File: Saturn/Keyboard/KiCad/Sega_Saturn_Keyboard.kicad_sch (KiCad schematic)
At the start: 88 parts, among them SW1 RH CTRL, SW10 PRINT SCREEN, SW11 SCROLL LOCK, SW12 PAUSE, SW13 ? /, SW14 _ \, SW15 UP, SW16 LEFT, SW17 DOWN, SW18 RIGHT, SW19 PAGE DOWN, SW2 LH CTRL, SW20 PAGE UP, SW21 > ., SW22 無変換, SW23 カタカナ, SW24 前候補, SW25 SPACE, SW26 Z, SW27 END, SW28 K, SW29 L, SW3 RH SHIFT, SW30 + ;, SW31 * :, SW32 } ], SW33 ENTER, SW34 X, SW35 HOME, SW36 I, SW37 O, SW38 P, SW39 ' @, SW4 LH SHIFT, SW40 { [, SW41 DELETE, SW42 A, SW43 INSERT, SW44 ( 8, SW45 ) 9, SW46 ~ 0, SW47 = -, SW48 _ ^, SW49 | ¥, SW5 F8, SW50 S, SW51 BACKSPACE, SW52 < ,, SW53 M, SW54 N, SW55 B, SW56 V, SW57 C, SW58 J, SW59 H, SW6 F9, SW60 G, SW61 F, SW62 D, SW63 CAPS LOCK, SW64 U, SW65 Y, SW66 T, SW67 R, SW68 W, SW69 TAB, SW7 F10, SW70 E, SW71 半角/全角, SW72 ' 7, SW73 & 6, SW74 % 5, SW75 $ 4, SW76 # 3, SW77 " 2, SW78 Q, SW79 ! 1, SW8 F11, SW80 F7, SW81 F6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

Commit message: Initial PCB routing completed
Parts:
- added C1: 10µF, Capacitor_THT:CP_Radial_D8.0mm_P2.50mm, symbol Device:C_Polarized
- added CN1: Saturn, Connector_Dsub:DSUB-9_Pins_Horizontal_P2.77x2.84mm_EdgePinOffset7.70mm_Housed_MountingHolesOffset9.12mm, symbol Connector:DE9_Pins_MountingHoles
- added H1, H2, H3, H4, H5, H6: MountingHole, MountingHole:MountingHole_3.2mm_M3, symbol Mechanical:MountingHole
- added RN1: 10KΩ, Resistor_THT:R_Array_SIP9, symbol Device:R_Network08
- added RN2: R_Network07, Resistor_THT:R_Array_SIP8, symbol Device:R_Network07
- added SW84: F3, PCM_Switch_Keyboard_Cherry_MX:SW_Cherry_MX_PCB_1.00u, symbol Switch:SW_Push_45deg
- added U1: Teensy4.1, Clueless_Engineer:Teensy41, symbol teensy:Teensy4.1
- renumbered SW84 to SW85, SW85 to SW86, SW86 to SW87, SW87 to SW88, SW88 to SW89
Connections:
- net COL 16: now also RN1.2 (R1), U1.24 (32_OUT1B)
- net COL 17: now also RN1.3 (R2), U1.23 (31_CTX3)
- net COL 18: now also RN1.4 (R3), U1.22 (30_CRX3)
- net COL 19: now also RN1.5 (R4), SW84.1, U1.21 (29_TX7)
- net COL 20: now also RN1.6 (R5), U1.20 (28_RX7)
- net COL 21: now also RN1.7 (R6), U1.19 (27_A13_SCK1)
- net COL 22: now also RN1.8 (R7), U1.18 (26_A12_MOSI1)
- net COL 23: now also RN1.9 (R8), U1.17 (25_A11_RX6_SDA2)
- net ROW 1: now also U1.45 (23_A9_CRX1_MCLK1)
- net ROW 10: now also U1.8 (6_OUT1D)
- net ROW 11: now also U1.7 (5_IN2)
- net ROW 12: now also U1.6 (4_BCLK2)
- net ROW 13: now also SW84.2, U1.5 (3_LRCLK2)
- net ROW 14: now also U1.44 (22_A8_CTX1)
- net ROW 2: now also U1.43 (21_A7_RX5_BCLK1)
- net ROW 3: now also U1.11 (9_OUT1C)
- net ROW 4: now also U1.14 (12_MISO_MQSL)
- net ROW 5: now also U1.4 (2_OUT2)
- net ROW 6: now also U1.13 (11_MOSI_CTX1)
- net ROW 7: now also U1.12 (10_CS_MQSR)
- net ROW 8: now also U1.10 (8_TX2_IN1)
- net ROW 9: now also U1.9 (7_RX2_OUT1A)
- new net +5V_{OUT}: C1.1, CN1.1, RN1.1 (common), RN2.1 (common), U1.48 (VIN)
- new net D_{D1}: CN1.2, RN2.3 (R2), U1.30 (38_CS1_IN1)
- new net GND: C1.2, CN1.0 (PAD), CN1.9, U1.1 (GND), U1.34 (GND), U1.47 (GND), U1.52 (GND)
- new net L_{D2}: CN1.8, RN2.6 (R5), U1.27 (35_TX8)
- new net R_{D3}: CN1.7, RN2.4 (R3), U1.29 (37_CS)
- new net TH_{S0}: CN1.4, RN2.7 (R6), U1.26 (34_RX8)
- new net TL: CN1.6, RN2.2 (R1), U1.31 (39_MISO1_OUT1A)
- new net TR_{S1}: CN1.5, RN2.8 (R7), U1.25 (33_MCLK2)
- new net U_{D0}: CN1.3, RN2.5 (R4), U1.28 (36_CS)
- no-connect marks 0 -> 13

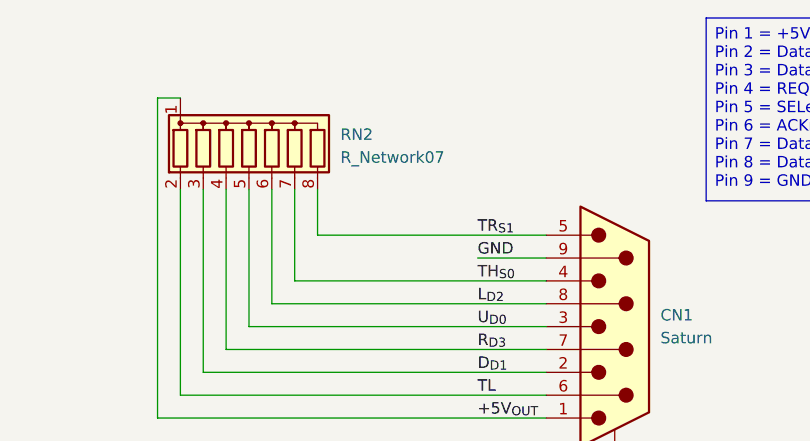
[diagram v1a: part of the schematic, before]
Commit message: Added 100KΩ value for pull-up
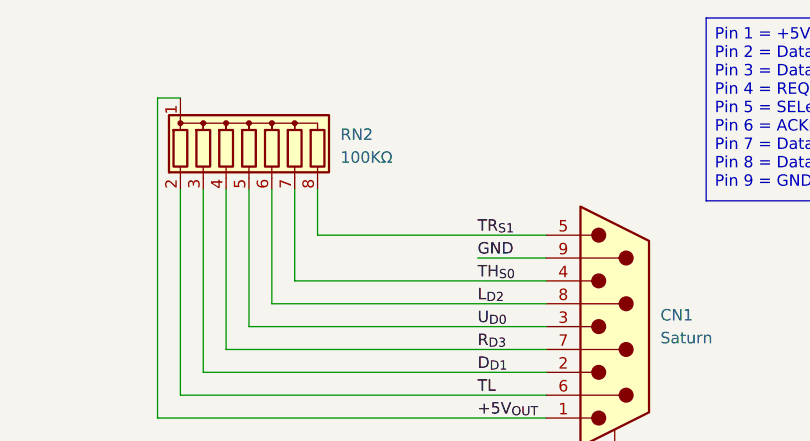
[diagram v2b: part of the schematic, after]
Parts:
- RN2: value R_Network07 -> 100KΩ
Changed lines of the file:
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@@
 			)
 		)
-		(property "Value" "R_Network07"
+		(property "Value" "100KΩ"
 			(at 334.01 32.0039 0)
 			(effects

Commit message: Additional text on PCB
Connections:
- no-connect marks 13 -> 28
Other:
- moved on the sheet: CN1, H1, H2, H3, H4, H5, H6, RN2

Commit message: Update Sega_Saturn_Keyboard.kicad_sch
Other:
- note added: "-->"
- note added: "<--"
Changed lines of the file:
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@@
 		(comment 2 "github.com/BrettHallen")
+	)
+	(text "<--"
+		(exclude_from_sim no)
+		(at 332.486 41.148 0)
+		(effects
+			(font
+				(size 1.27 1.27)
+			)
+		)
+	)
+	(text "<--"
+		(exclude_from_sim no)
+		(at 332.74 35.814 0)
+		(effects
+			(font
+				(size 1.27 1.27)
+			)
+		)
 	)
 	(text "Row & Column numbering correspond to the\nassigned CN2 pin inside the keyboard."
@@
 		)
 	)
+	(text "-->"
+		(exclude_from_sim no)
+		(at 332.994 53.594 0)
+		(effects
+			(font
+				(size 1.27 1.27)
+			)
+		)
+	)
+	(text_box "S0/TH/SELECT\nSaturn --> Controller\n\nS1/TR/REQUEST\nSaturn --> Controller\n\nTL/ACKNOWLEDGE\nSaturn <-- Controller"
+		(exclude_from_sim no)
+		(at 367.03 66.04 0)
+		(size 35.56 20.32)
+		(margins 0.9525 0.9525 0.9525 0.9525)
+		(stroke
+			(width 0)
+			(type solid)
+		)
+		(fill
+			(type none)
+		)
+		(effects
+			(font
+				(size 1.27 1.27)
+			)
+			(justify left top)
+		)
+	)

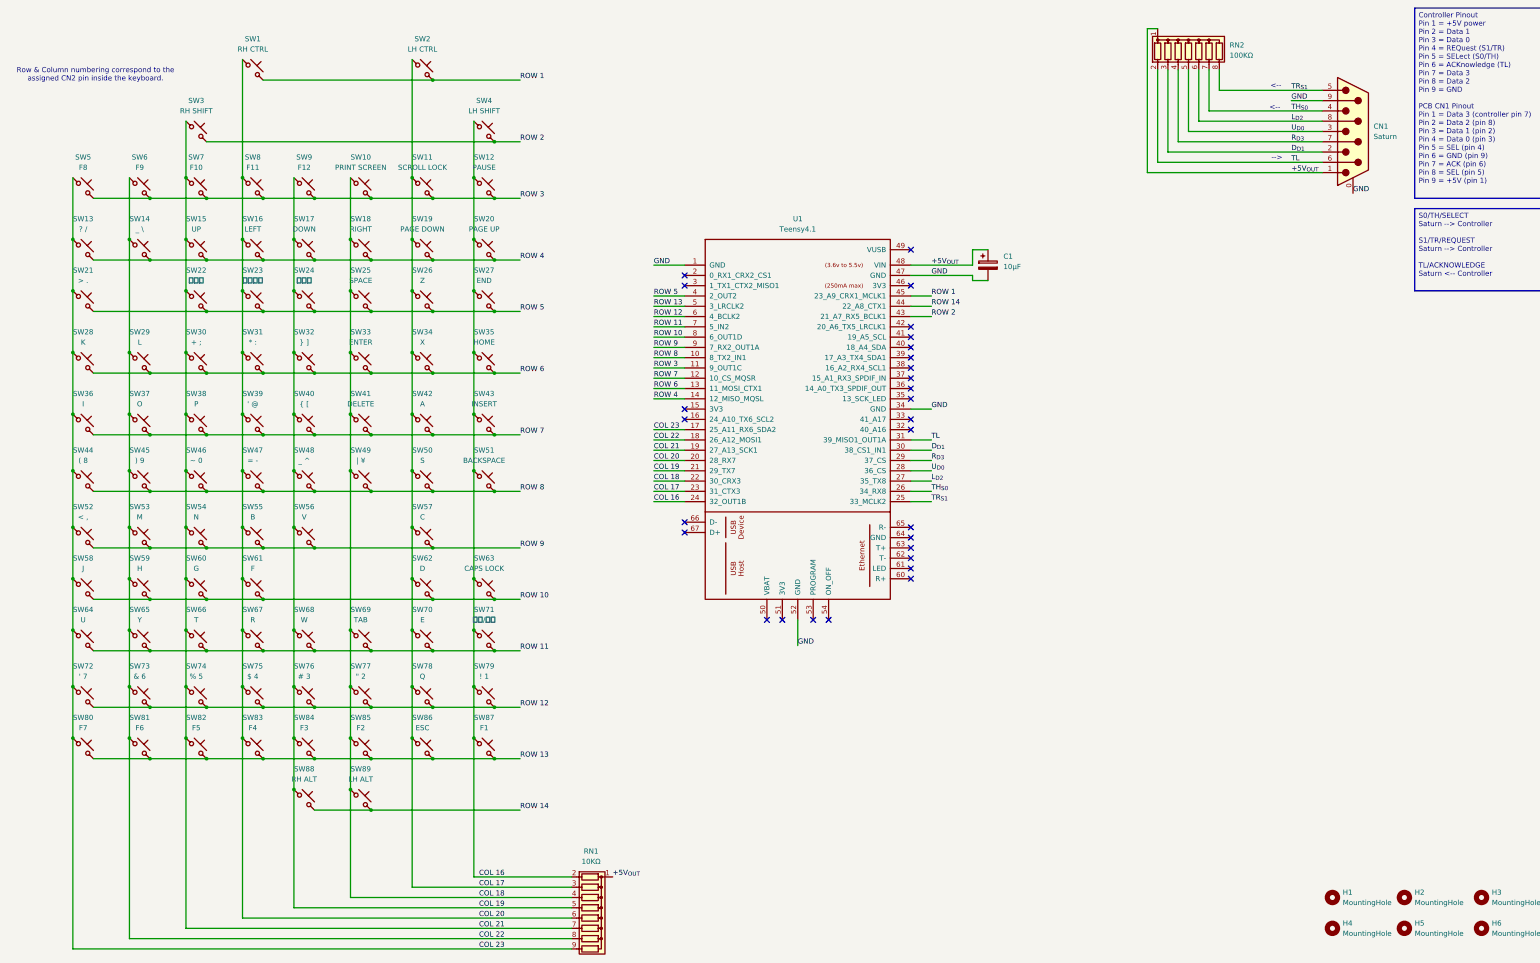
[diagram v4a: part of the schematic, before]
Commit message: Swapped DE9 male -> female
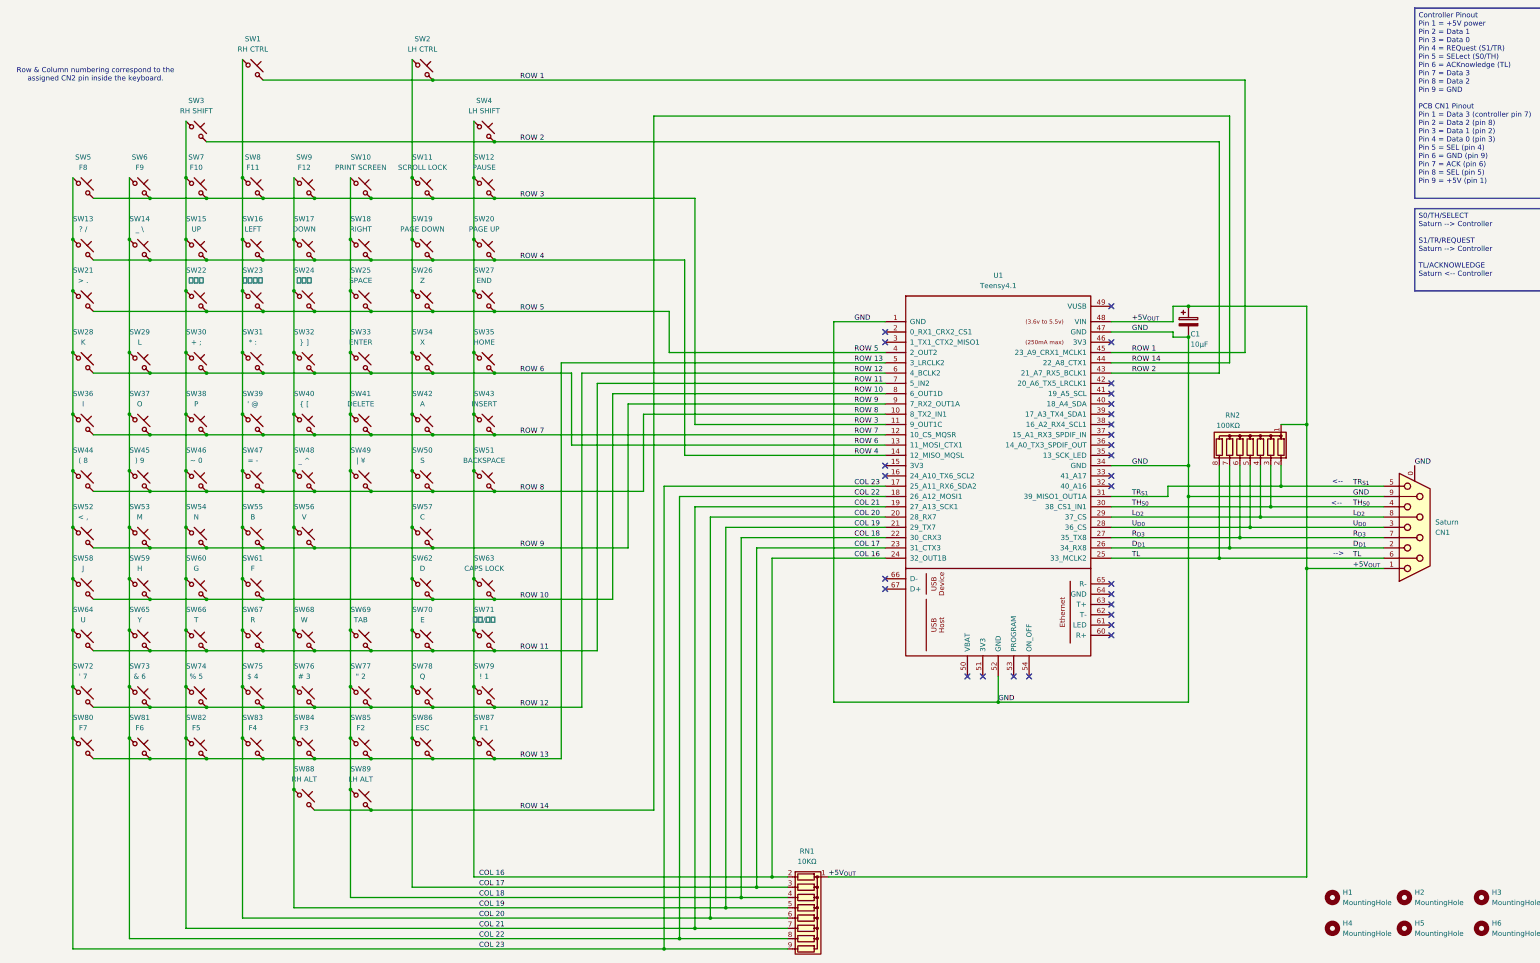
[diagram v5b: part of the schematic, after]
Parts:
- removed CN1: Saturn, Connector_Dsub:DSUB-9_Pins_Horizontal_P2.77x2.84mm_EdgePinOffset7.70mm_Housed_MountingHolesOffset9.12mm, symbol Connector:DE9_Pins_MountingHoles
- added CN1: Saturn, Connector_Dsub:DSUB-9_Socket_Horizontal_P2.77x2.84mm_EdgePinOffset7.70mm_Housed_MountingHolesOffset9.12mm, symbol Connector:DE9_Socket_MountingHoles
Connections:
- net +5V_{OUT}: now also CN1.1
- net D_{D1}: now also RN2.7 (R6), U1.26 (34_RX8), CN1.2; no longer RN2.3 (R2), U1.30 (38_CS1_IN1)
- net GND: now also CN1.0 (PAD), CN1.9
- net L_{D2}: now also RN2.4 (R3), U1.29 (37_CS), CN1.8; no longer RN2.6 (R5), U1.27 (35_TX8)
- net R_{D3}: now also RN2.6 (R5), U1.27 (35_TX8), CN1.7; no longer RN2.4 (R3), U1.29 (37_CS)
- net TH_{S0}: now also RN2.3 (R2), U1.30 (38_CS1_IN1), CN1.4; no longer RN2.7 (R6), U1.26 (34_RX8)
- net TL: now also RN2.8 (R7), U1.25 (33_MCLK2), CN1.6; no longer RN2.2 (R1), U1.31 (39_MISO1_OUT1A)
- net TR_{S1}: now also RN2.2 (R1), U1.31 (39_MISO1_OUT1A), CN1.5; no longer RN2.8 (R7), U1.25 (33_MCLK2)
- net U_{D0}: now also CN1.3
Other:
- moved on the sheet: C1, RN1, RN2, U1

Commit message: Design tweaks
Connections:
- net GND: no longer U1.52 (GND)
- no-connect marks 28 -> 18
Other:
- note added: "←"
- note added: "→"
- note removed: "-->"
- note removed: "<--"
